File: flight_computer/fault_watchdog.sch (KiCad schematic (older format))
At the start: 18 parts

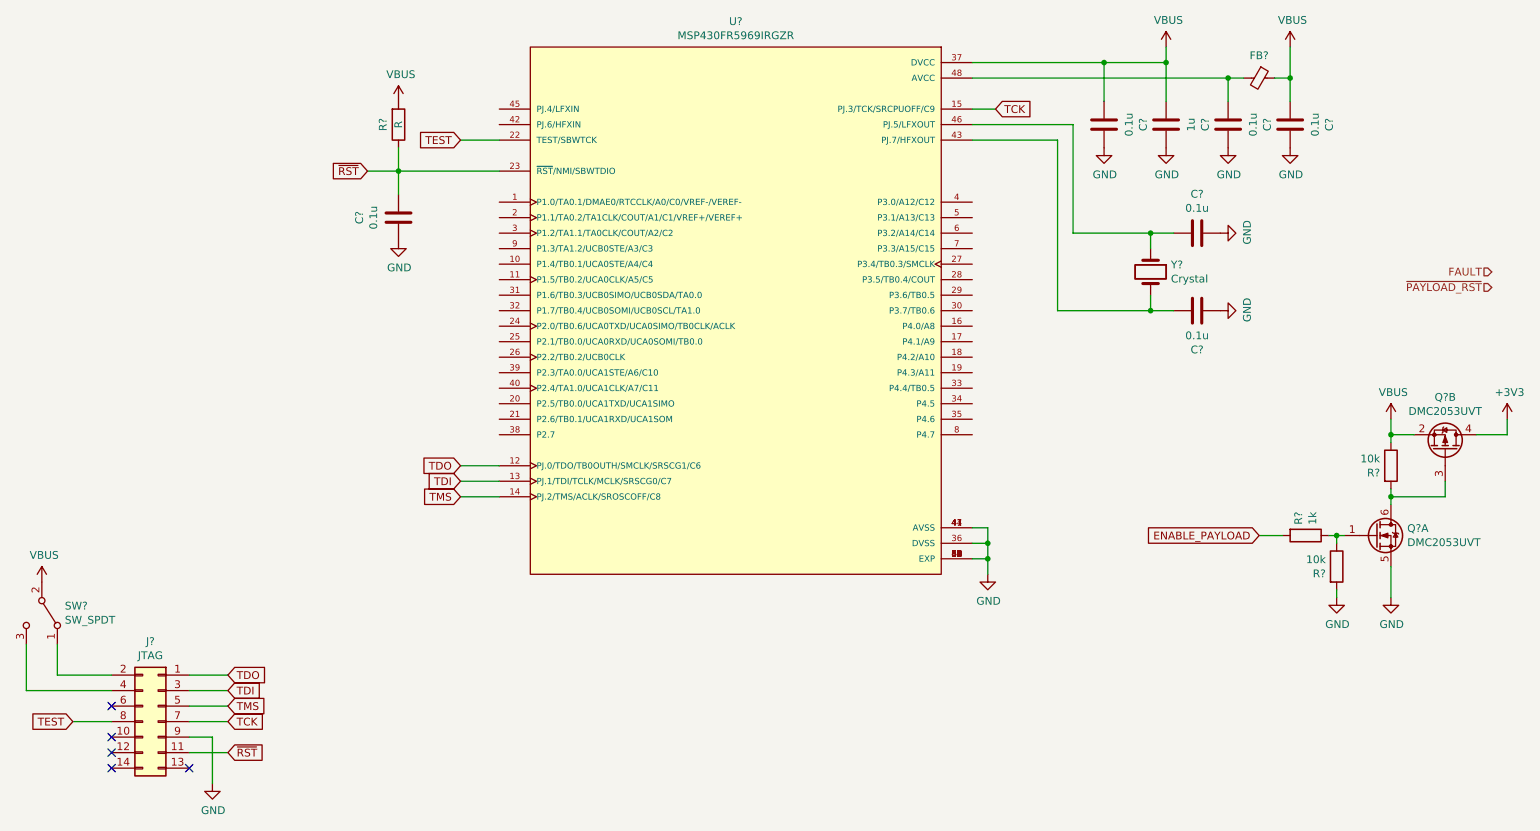
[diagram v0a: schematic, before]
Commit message: Annotating schematic with references and footprints
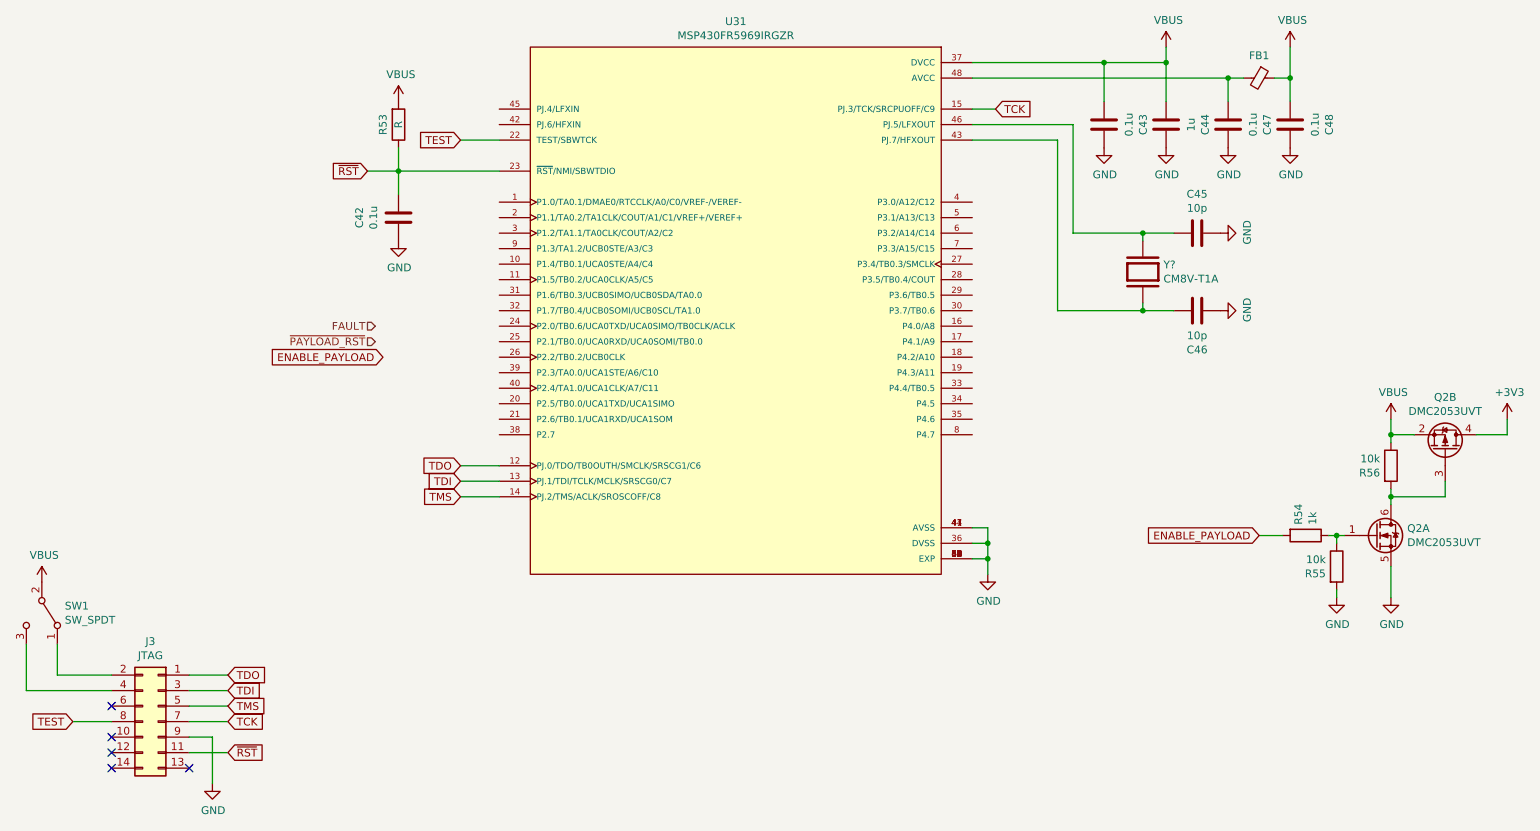
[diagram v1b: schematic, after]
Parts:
- removed Y?: Crystal, symbol Device:Crystal
- added Y?: CM8V-T1A, XTAL_CM8V-T1A-32.768KHZ-7PF-20PPM-TA-QC, symbol CM8V-T1A-32.768KHZ-7PF-20PPM-TA-QC:CM8V-T1A-32.768KHZ-7PF-20PPM-TA-QC
- C45, C46: renamed from C?; value 0.1u -> 10p
- U31: renamed from U?; footprint QFN50P700X700X100-49N -> MSP430FR5969IRGZR:QFN50P700X700X100-49N
- gave numbers to parts that had none: 13
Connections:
- net at C46.2, U31.43 (PJ.7/HFXOUT): now also Y?.2
- net at C45.2, U31.46 (PJ.5/LFXOUT): now also Y?.1
